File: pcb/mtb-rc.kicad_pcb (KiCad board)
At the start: 4 copper layers, 100 x 70 mm, 166 parts, among them J1 MVE252-5-V, J10 MVE252-5-V, J11 MVE252-5-V, J2 MVE252-5-V, J3 MVE252-5-V, J4 MVE252-5-V, J5 MVE252-5-V, J6 PINHEADER, J7 PINHEADER, J8 PROG/DEBUG, J9 MVE252-5-V, SW1 6x6, U1 VO0631T, U10 LM339, U11 LM339, U12 STM32F103C8Tx, U13 HT7533-1, U14 78M05, U15 MAX487, U2 VO0631T, U3 VO0631T, U4 L78L05_SOT89, U5 L79L05_SOT89, U6 LM339, U7 LM339, U8 LM339, U9 4052, Y1 14.7456MHz

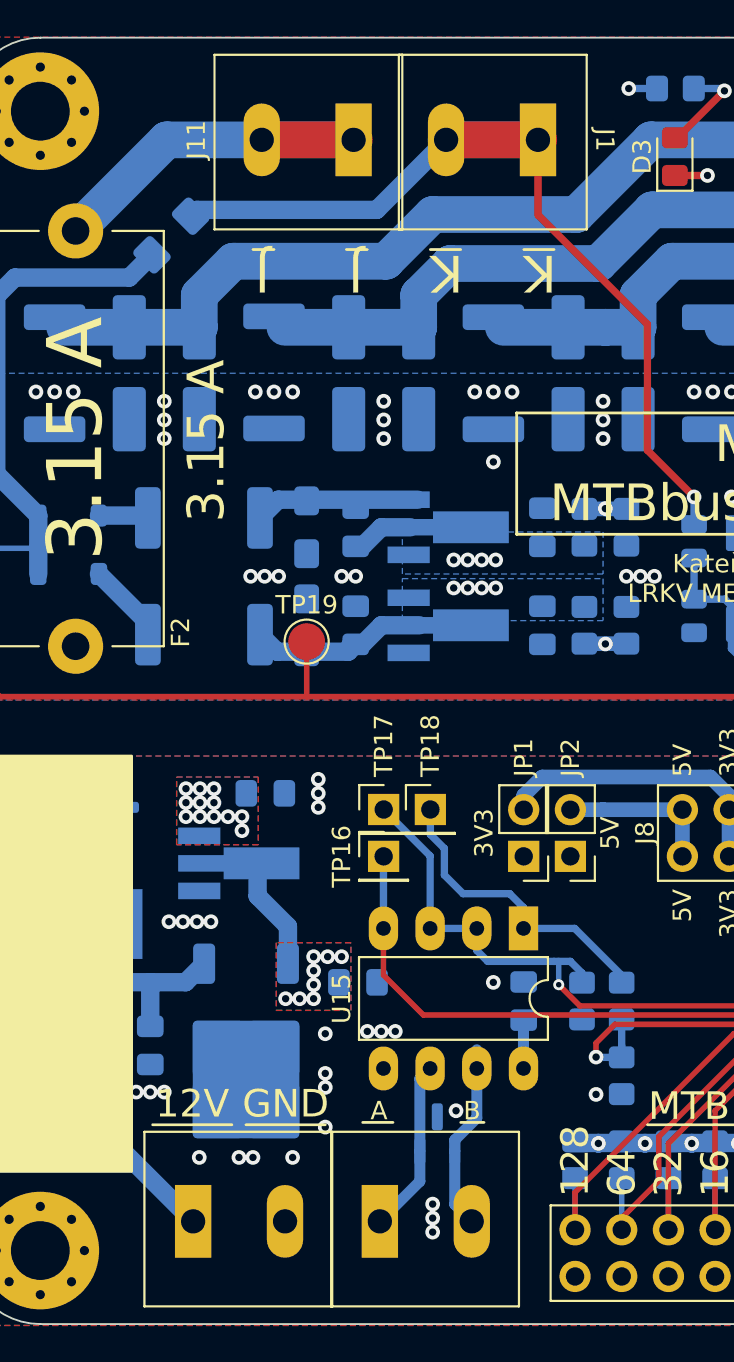
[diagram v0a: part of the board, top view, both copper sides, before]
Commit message: Use 2×MVE252-5-V footprint.
To avoid DRC issues in PCB.
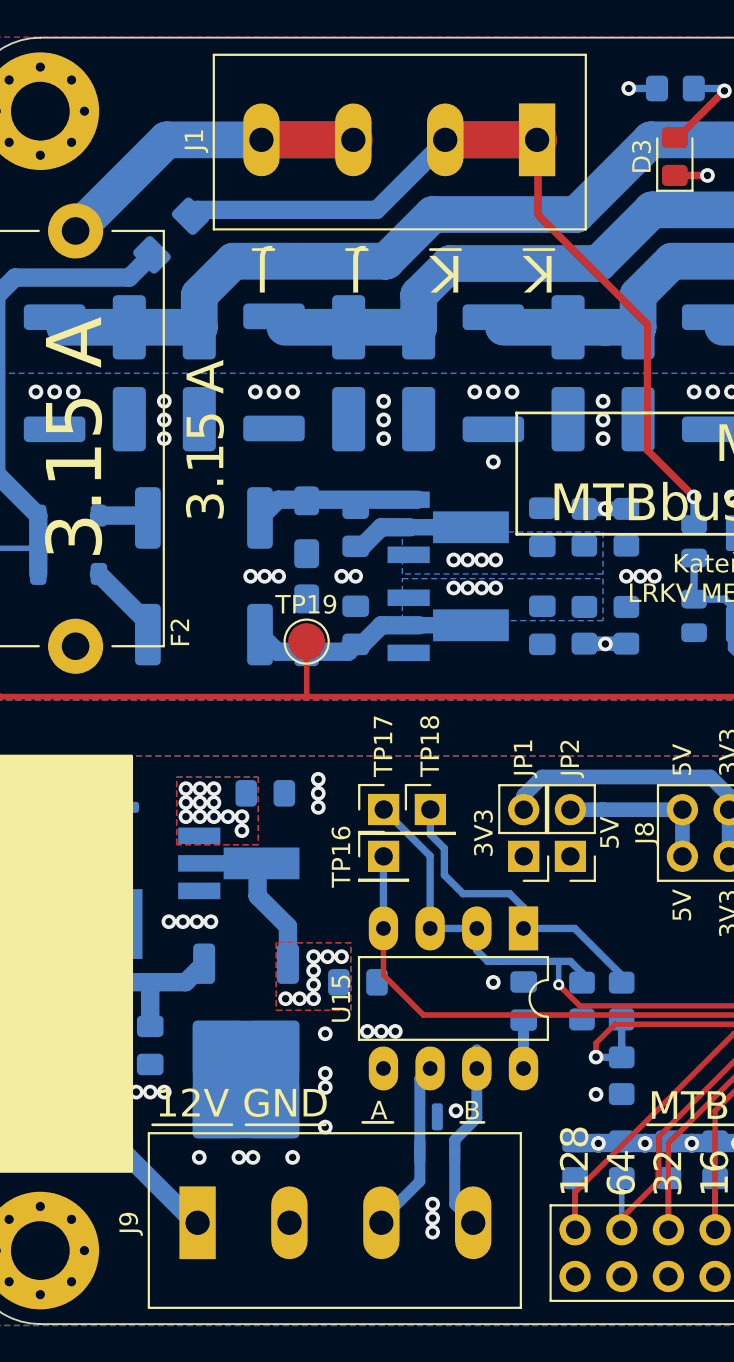
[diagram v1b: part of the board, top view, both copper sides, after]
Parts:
- removed J10, J11: MVE252-5-V, TerminalBlock_Euroclamp:MVE252-5-V
- J1, J9: footprint TerminalBlock_Euroclamp:MVE252-5-V -> TerminalBlock_Euroclamp:MVE252-5-V-2x
- R39: value 1k -> 2k2
- R41: value 1k -> 10k
- moved J9 5.15 mm to (127.9, 94.7)
- moved J1 4.95 mm to (131.6, 35.3)

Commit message: v1.0 -> v1.1.
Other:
- board text added: "MTB-RC v1.1 MTBbus RailCom detector"
- board text removed: "MTB-RC v1.0 MTBbus RailCom detector"
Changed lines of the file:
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@@
     (effects (font (size 2 2) (thickness 0.2)))
   )
-  (gr_text "MTB-RC v1.0\nMTBbus RailCom detector" (at 157.48 53.721) (layer "F.SilkS")
+  (gr_text "MTB-RC v1.1\nMTBbus RailCom detector" (at 157.48 53.721) (layer "F.SilkS")
     (effects (font (size 2 2) (thickness 0.25)))
   )

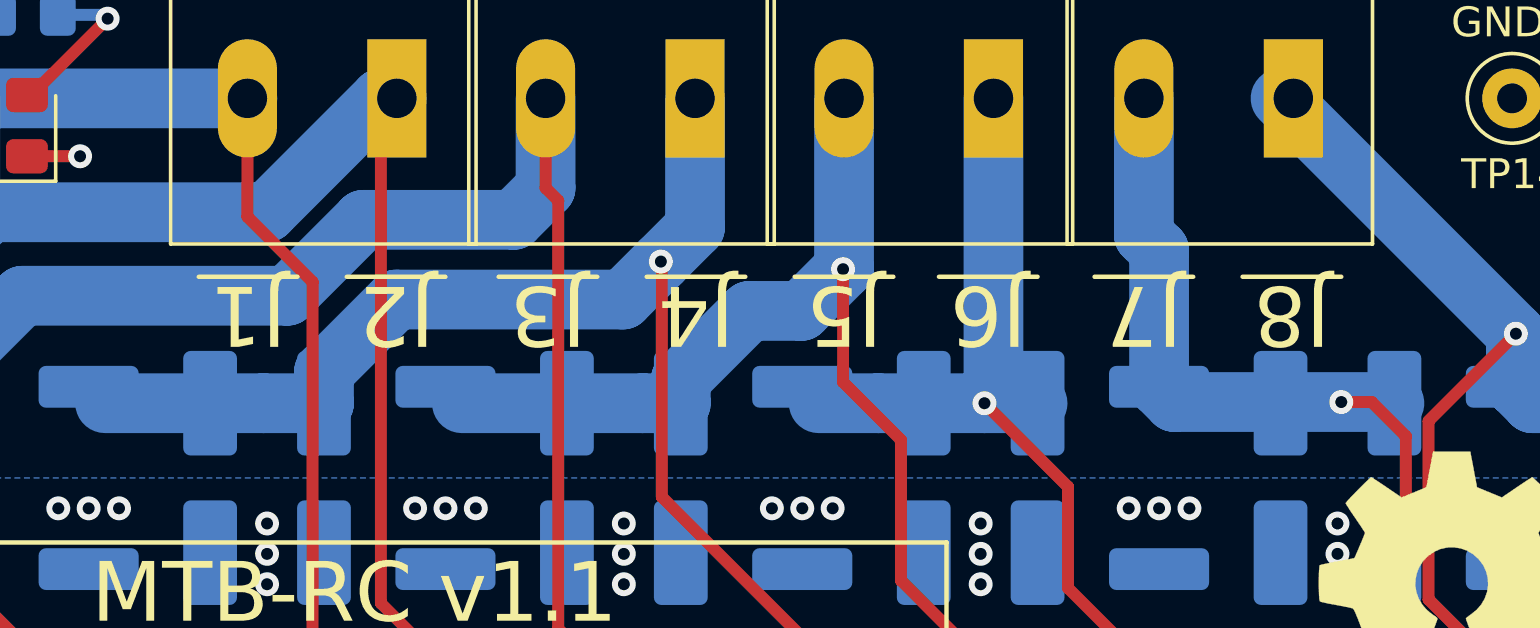
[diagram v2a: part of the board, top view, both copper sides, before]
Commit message: J1-J8 -> J0-J7.
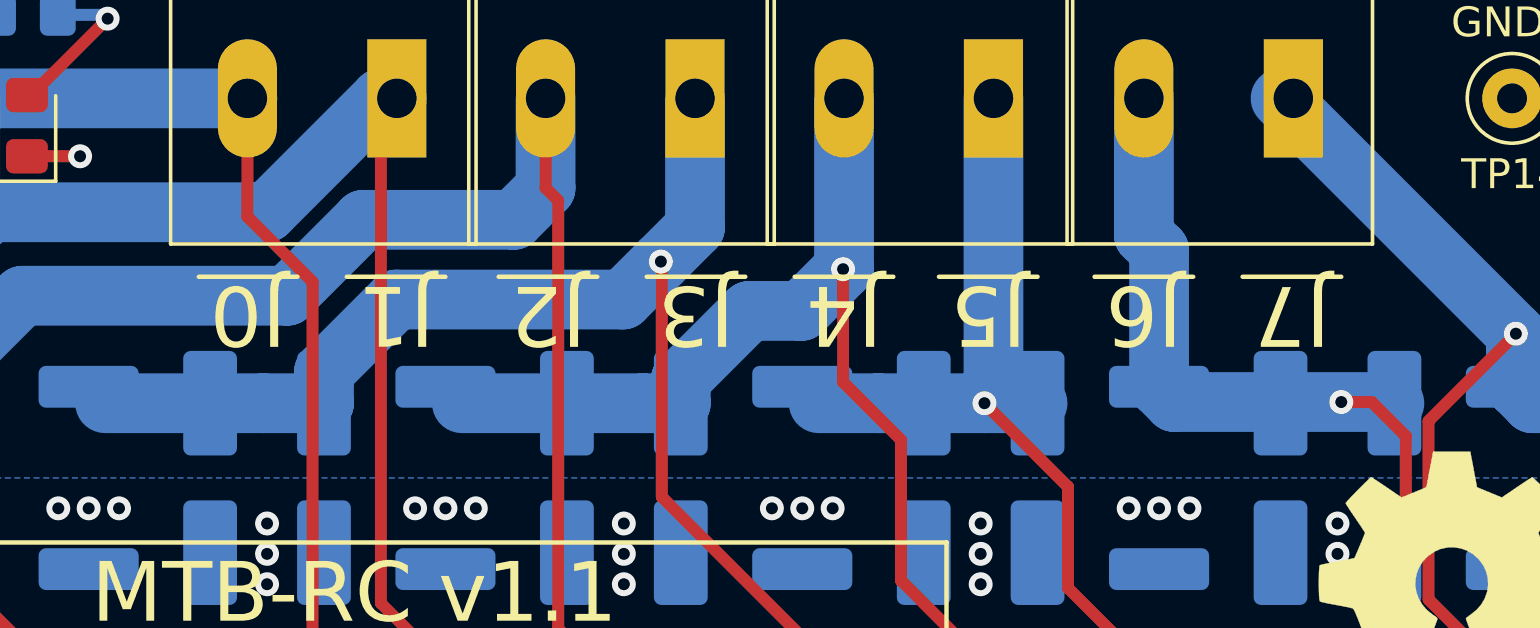
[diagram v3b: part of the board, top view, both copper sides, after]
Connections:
- net /DCC/RC1 renamed Net-(U6A--)
- D11 pad 2: /DCC/J1 -> /DCC/J0
- D12 pad 1: /DCC/J1 -> /DCC/J0
- D13 pad 2: /DCC/J2 -> /DCC/J1
- D14 pad 1: /DCC/J2 -> /DCC/J1
- D15 pad 2: /DCC/J3 -> /DCC/J2
- D16 pad 1: /DCC/J3 -> /DCC/J2
- D17 pad 2: /DCC/J4 -> /DCC/J3
- D18 pad 1: /DCC/J4 -> /DCC/J3
- D19 pad 1: /DCC/J5 -> /DCC/J4
- D20 pad 2: /DCC/J5 -> /DCC/J4
- D21 pad 1: /DCC/J6 -> /DCC/J5
- D22 pad 2: /DCC/J6 -> /DCC/J5
- D23 pad 1: /DCC/J7 -> /DCC/J6
- D24 pad 2: /DCC/J7 -> /DCC/J6
- D25 pad 1: /DCC/J8 -> /DCC/J7
- D26 pad 2: /DCC/J8 -> /DCC/J7
- J2 pad 1: /DCC/J2 -> /DCC/J1
- J2 pad 2: /DCC/J1 -> /DCC/J0
- J3 pad 1: /DCC/J4 -> /DCC/J3
- J3 pad 2: /DCC/J3 -> /DCC/J2
- J4 pad 1: /DCC/J6 -> /DCC/J5
- J4 pad 2: /DCC/J5 -> /DCC/J4
- J5 pad 1: /DCC/J8 -> /DCC/J7
- J5 pad 2: /DCC/J7 -> /DCC/J6
- R14 pad 1: /DCC/J1 -> /DCC/J0
- R15 pad 1: /DCC/J2 -> /DCC/J1
- R16 pad 1: /DCC/J3 -> /DCC/J2
- R17 pad 1: /DCC/J4 -> /DCC/J3
- R20 pad 1: /DCC/J1 -> /DCC/J0
- R21 pad 1: /DCC/J2 -> /DCC/J1
- R22 pad 1: /DCC/J3 -> /DCC/J2
- R23 pad 1: /DCC/J4 -> /DCC/J3
- R31 pad 1: /DCC/J5 -> /DCC/J4
- R32 pad 1: /DCC/J6 -> /DCC/J5
- R33 pad 1: /DCC/J7 -> /DCC/J6
- R34 pad 1: /DCC/J8 -> /DCC/J7
- R35 pad 1: /DCC/J5 -> /DCC/J4
- R36 pad 1: /DCC/J6 -> /DCC/J5
- R37 pad 1: /DCC/J7 -> /DCC/J6
- R38 pad 1: /DCC/J8 -> /DCC/J7
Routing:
- net /DCC/J0: track 0.00 -> 75.8 mm, vias 0 -> 1
- net /DCC/J8: track 35.6 -> 0.00 mm, vias 2 -> 0
- net /DCC/J3: track 64.5 -> 43.8 mm, vias 1 -> 2
- net /DCC/J5: track 45.6 -> 30.0 mm
- net /DCC/J1: track 75.8 -> 61.2 mm
- net /DCC/J6: track 30.0 -> 36.7 mm
- net /DCC/J2: track 61.2 -> 64.5 mm
- net /DCC/J4: track 43.8 -> 45.6 mm
- net /DCC/J7: track 36.7 -> 35.6 mm
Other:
- board text added: "J0"
- board text removed: "J8"

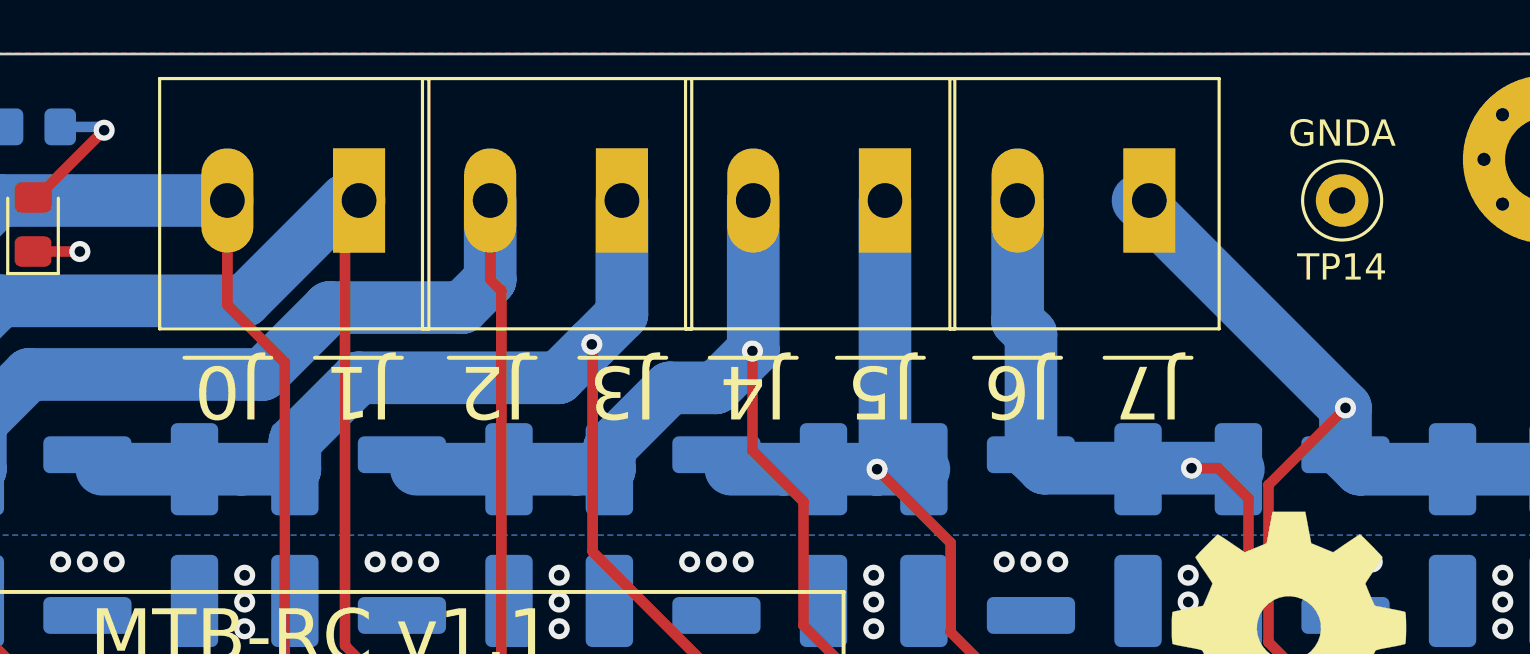
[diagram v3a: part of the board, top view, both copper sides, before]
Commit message: Use 4×MVE252-5-V footprint.
To avoid DRC issues in schematics.
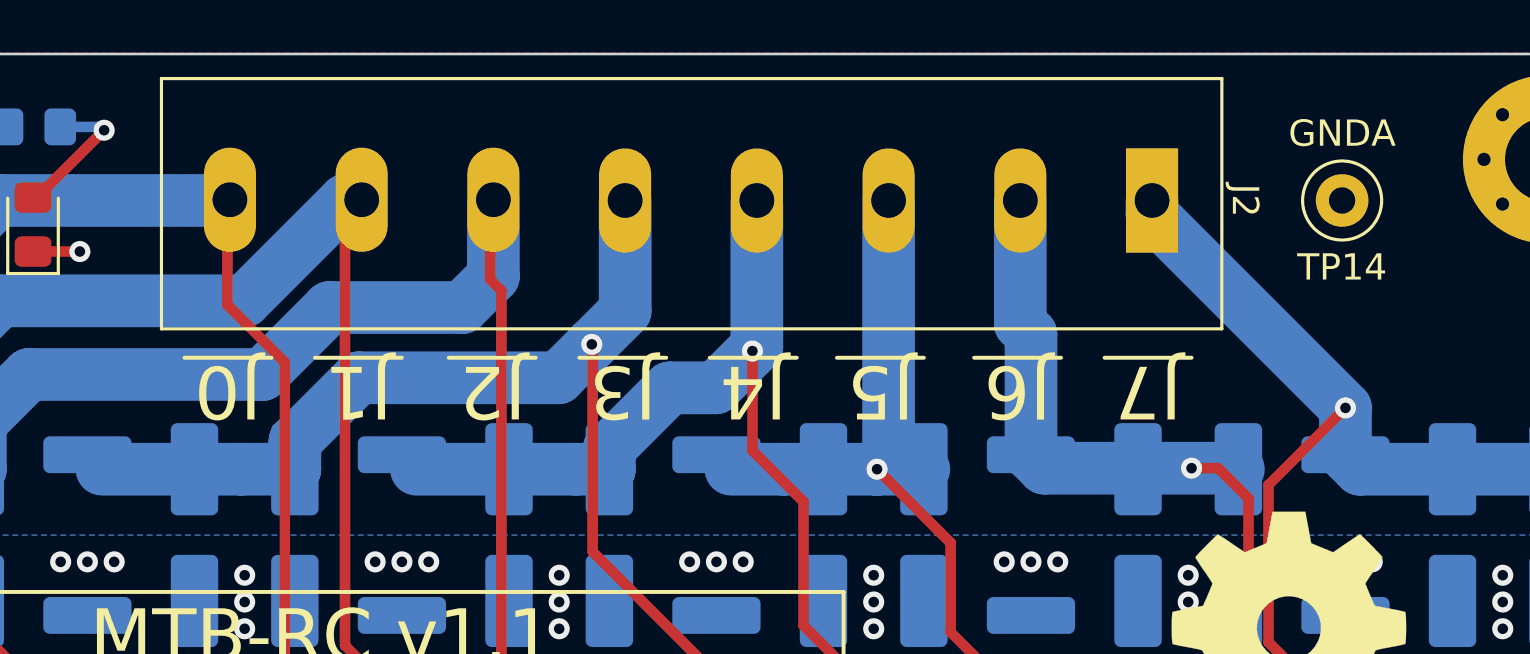
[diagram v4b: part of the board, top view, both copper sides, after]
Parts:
- removed J3, J4, J5: MVE252-5-V, TerminalBlock_Euroclamp:MVE252-5-V
- J2: footprint TerminalBlock_Euroclamp:MVE252-5-V -> TerminalBlock_Euroclamp:MVE252-5-V-4x
- moved J2 32.6 mm to (189.0, 35.5)
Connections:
- J2 pad 1: /DCC/J1 -> /DCC/J7
- J2 pad 2: /DCC/J0 -> /DCC/J6

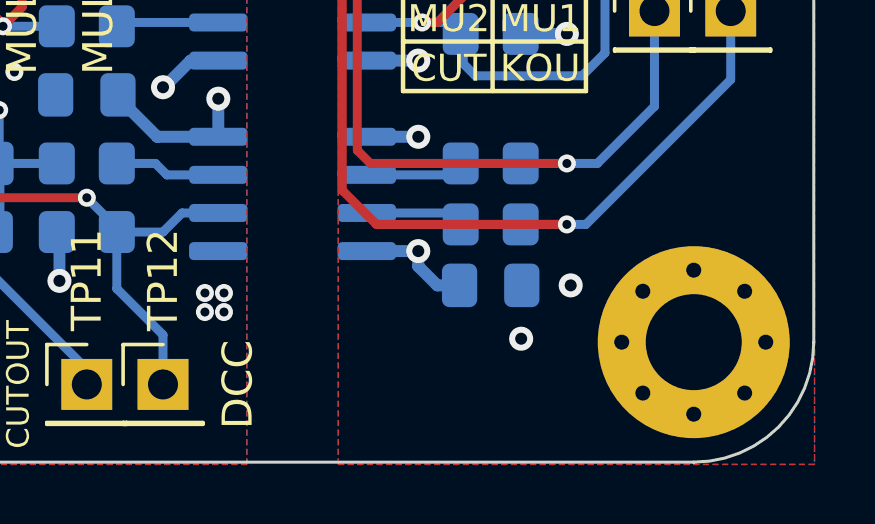
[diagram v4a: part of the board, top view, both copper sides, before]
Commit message: Add optocoupler-led protection diode. Close #1.
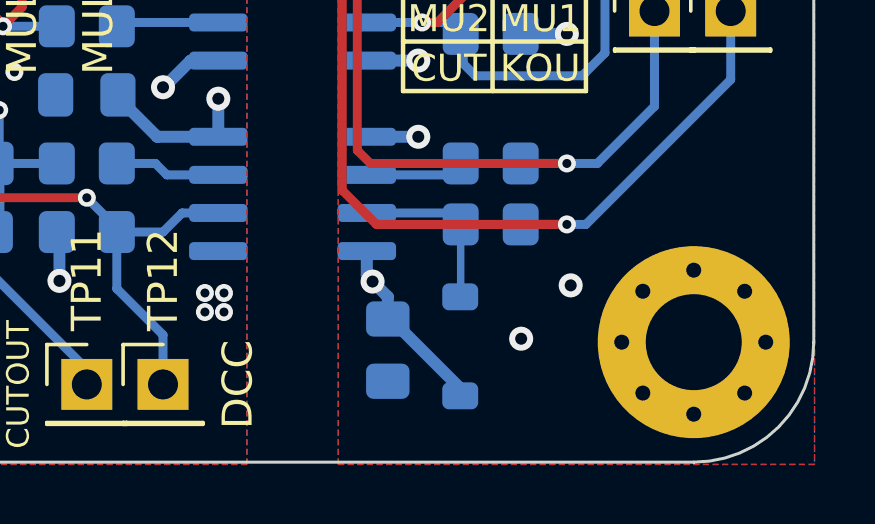
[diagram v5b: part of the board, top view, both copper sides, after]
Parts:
- added D27: 1N5819, Diode_SMD:D_SOD-123, B.Cu at (196.2, 96.1)
- D9: value 1N5819WS -> 1N5819
- moved C1 4.05 mm to (193.8, 96.3), turned to -90 degrees
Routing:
- net Net-(D27-A): track 3.37 -> 5.79 mm
- net +5VA: track 61.0 -> 63.2 mm
